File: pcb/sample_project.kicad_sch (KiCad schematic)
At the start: 1 part

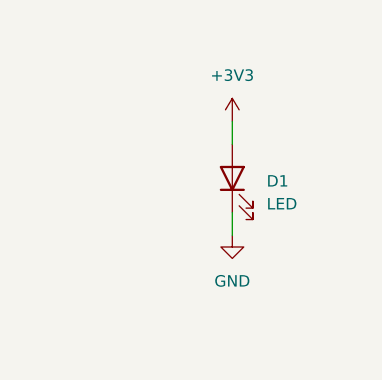
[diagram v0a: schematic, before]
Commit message: Updated exporting script
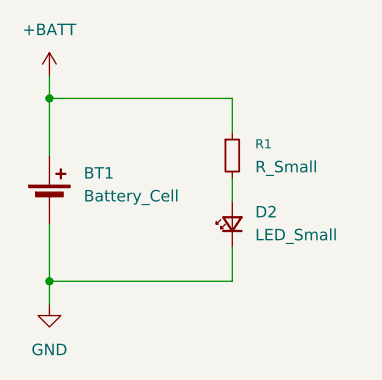
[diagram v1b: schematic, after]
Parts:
- removed D1: LED, LED_SMD:LED_0805_2012Metric, symbol Device:LED
- added BT1: Battery_Cell, Battery:BatteryHolder_Keystone_1060_1x2032, symbol Device:Battery_Cell
- added D2: LED_Small, LED_SMD:LED_0805_2012Metric, symbol Device:LED_Small
- added R1: R_Small, Resistor_SMD:R_0805_2012Metric, symbol Device:R_Small
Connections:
- net GND: now also BT1.2 (-), D2.1 (K)
- new net: D2.2 (A), R1.2
- new net +BATT: BT1.1 (+), R1.1
